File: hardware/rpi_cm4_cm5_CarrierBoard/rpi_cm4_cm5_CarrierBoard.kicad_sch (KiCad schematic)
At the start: 14 parts, among them J21 61300311121, J22 61300311121, U37 SN74LVC1G14DBVR

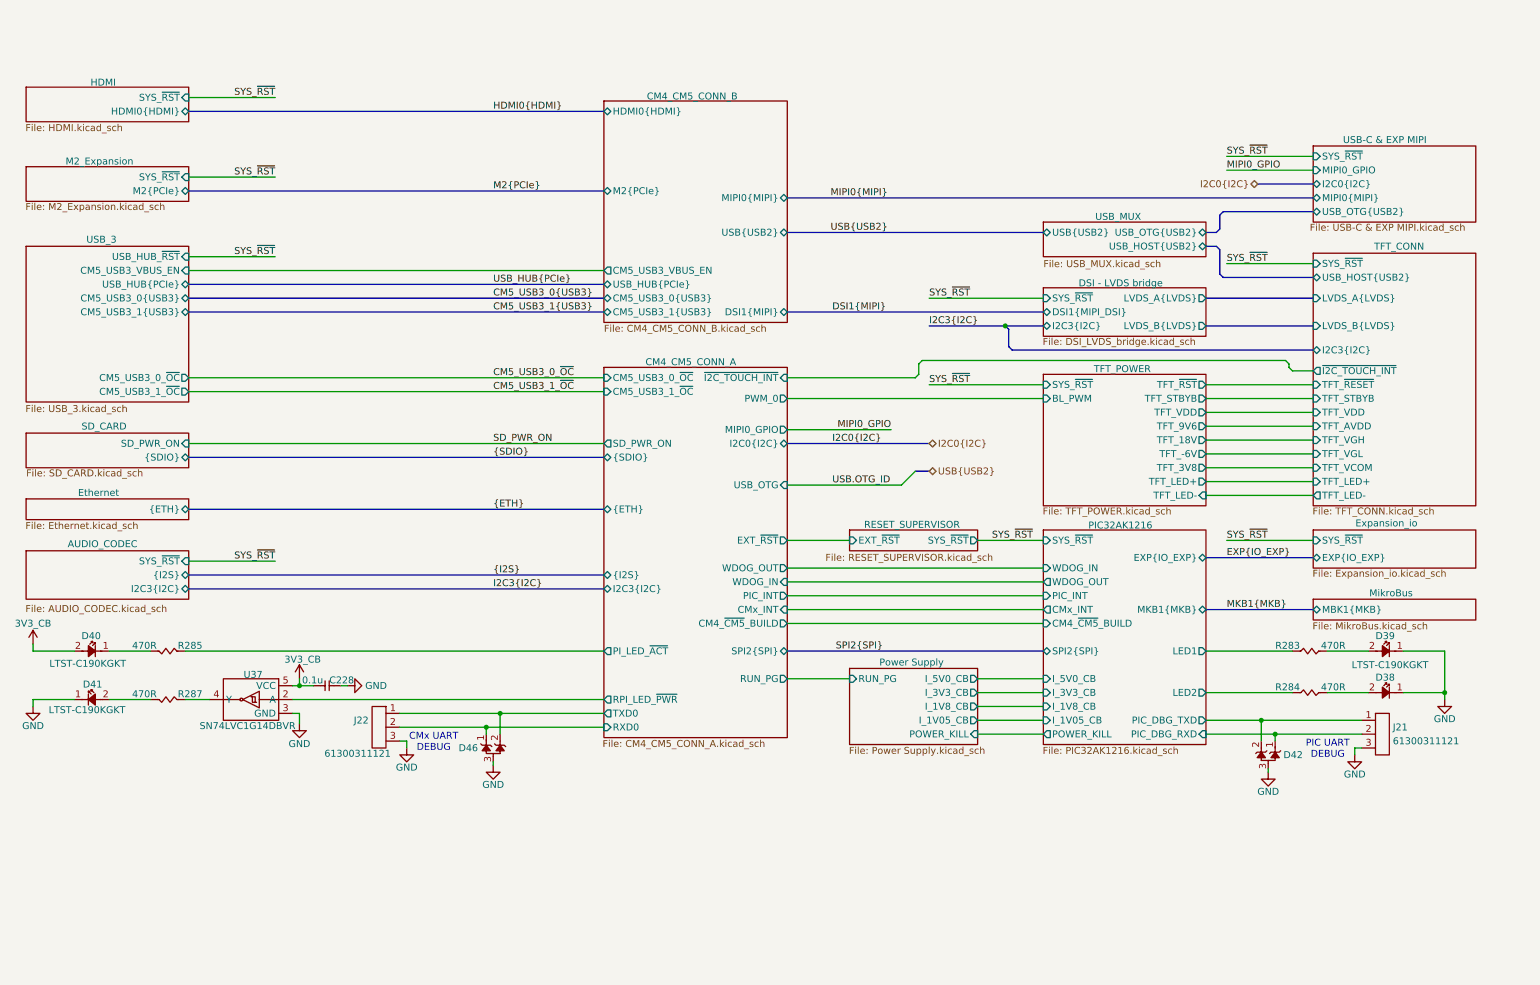
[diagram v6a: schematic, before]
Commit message: Added power input protection & filter Added dedicated QWIIC connector on RPI CMx I2C6 bus Adjusted power table and PinMux Updated schematics accordingly
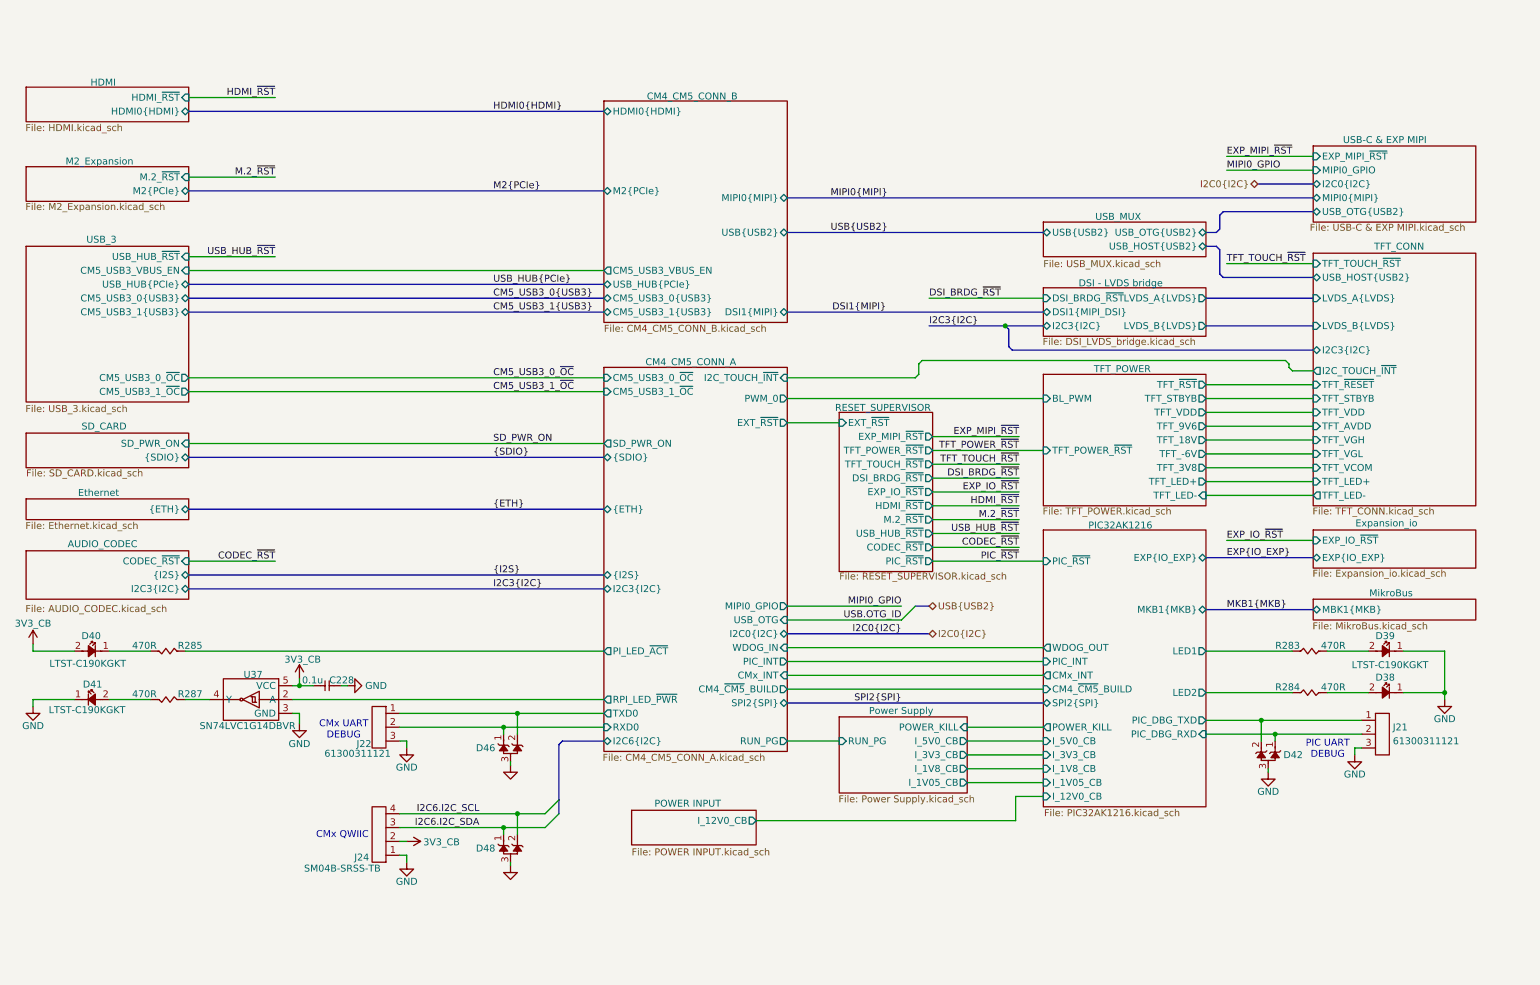
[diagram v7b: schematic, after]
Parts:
- added D48: D1213A-02SOL-7, footprint:SOT-23-3, symbol KicadCompDb:ESD Diodes/ESD_DIODE_00002
- added J24: SM04B-SRSS-TB, footprint:SM04B-SRSS-TB, symbol KicadCompDb:Connector/ONN_00023
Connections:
- net 3V3_CB: now also J24.2
- net GND: now also D48.3 (GND), J24.1
- new net I2C6.I2C_SCL: D48.2 (A), J24.4
- new net I2C6.I2C_SDA: D48.1, J24.3
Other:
- added sheet POWER INPUT (POWER INPUT.kicad_sch)
- sheet AUDIO_CODEC ports: added CODEC_~{RST}; removed SYS_~{RST}
- sheet CM4_CM5_CONN_A ports: added I2C6{I2C}, I2C_TOUCH_~{INT}; removed WDOG_OUT, ~{I2C_TOUCH_INT}
- sheet DSI - LVDS bridge ports: added DSI_BRDG_~{RST}; removed SYS_~{RST}
- sheet Expansion_io ports: added EXP_IO_~{RST}; removed SYS_~{RST}
- sheet HDMI ports: added HDMI_~{RST}; removed SYS_~{RST}
- sheet M2_Expansion ports: added M.2_~{RST}; removed SYS_~{RST}
- sheet PIC32AK1216 ports: added I_12V0_CB, PIC_~{RST}; removed SYS_~{RST}, WDOG_IN
- sheet RESET_SUPERVISOR ports: added CODEC_~{RST}, DSI_BRDG_~{RST}, EXP_IO_~{RST}, EXP_MIPI_~{RST}, HDMI_~{RST}, M.2_~{RST}, PIC_~{RST}, TFT_POWER_~{RST}, TFT_TOUCH_~{RST}, USB_HUB_~{RST}; removed SYS_~{RST}
- sheet TFT_CONN ports: added I2C_TOUCH_~{INT}, TFT_TOUCH_~{RST}; removed SYS_~{RST}, ~{I2C_TOUCH_INT}
- sheet TFT_POWER ports: added TFT_POWER_~{RST}; removed SYS_~{RST}
- sheet USB-C & EXP MIPI ports: added EXP_MIPI_~{RST}; removed SYS_~{RST}
- note added: "CMx QWIIC"
- moved on the sheet: D46

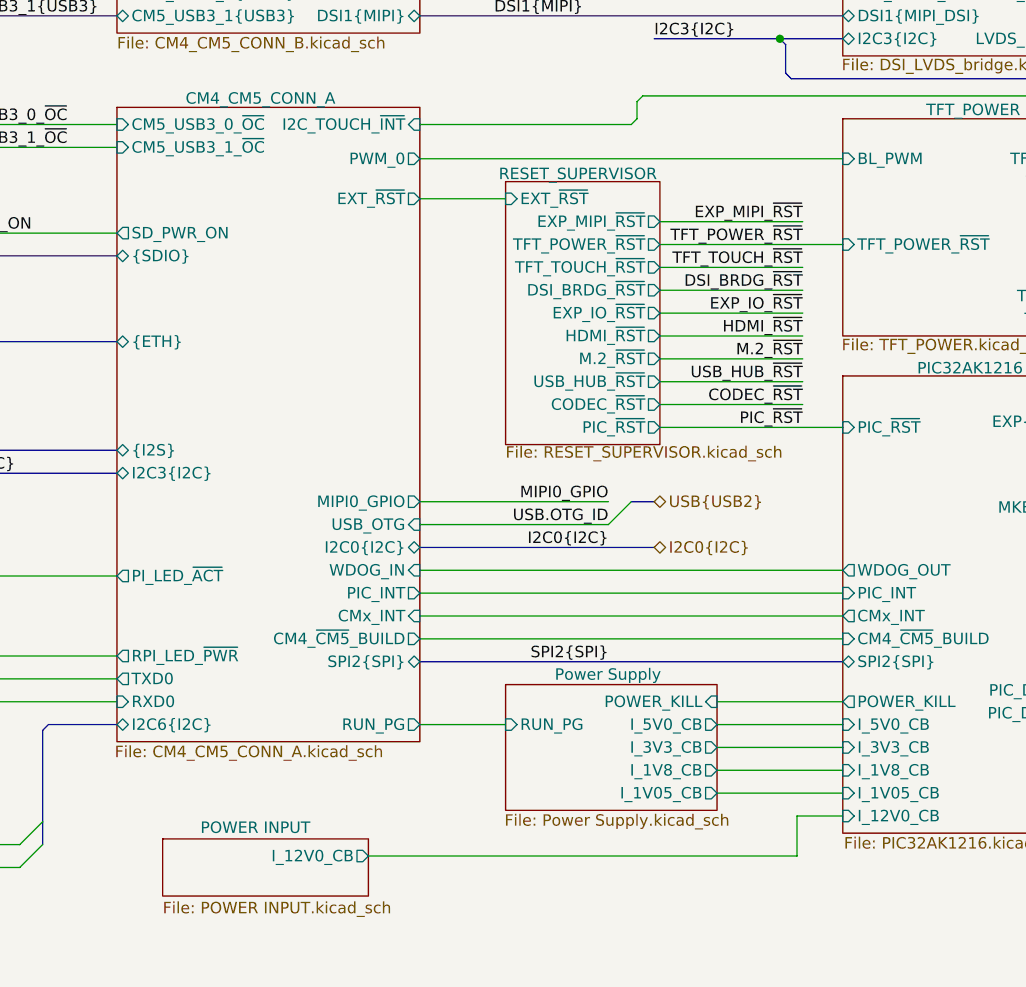
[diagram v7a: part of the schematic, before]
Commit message: Review watchdog timer circuit to prevent race condition during shutdown
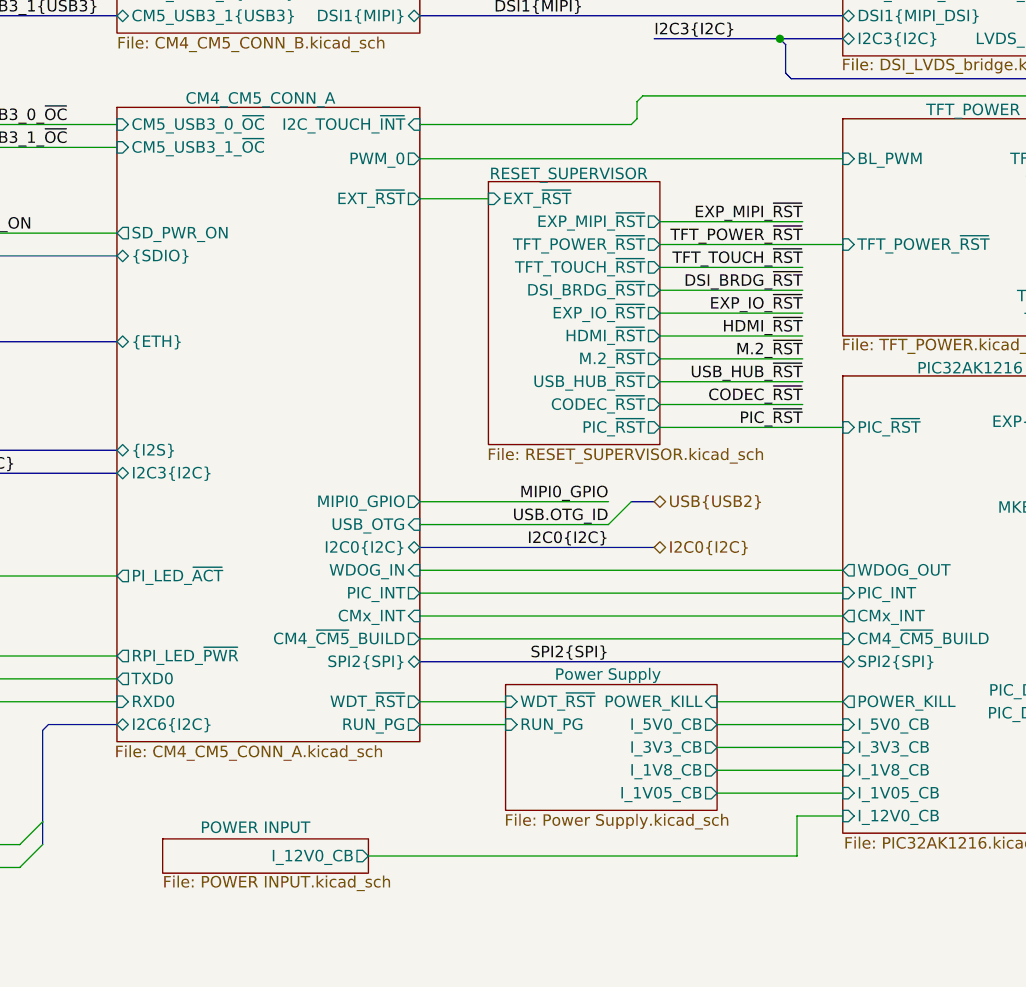
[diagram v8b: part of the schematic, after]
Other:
- sheet CM4_CM5_CONN_A ports: added WDT_~{RST}; removed none
- sheet Power Supply ports: added WDT_~{RST}; removed none
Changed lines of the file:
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@@
 	(wire
 		(pts
-			(xy 155.575 87.63) (xy 165.1 87.63)
-		)
-		(stroke
-			(width 0)
-			(type default)
-		)
-	)
-	(wire
-		(pts
 			(xy 236.22 38.735) (xy 252.095 38.735)
 		)
@@
 	(wire
 		(pts
+			(xy 155.575 143.51) (xy 165.1 143.51)
+		)
+		(stroke
+			(width 0)
+			(type default)
+		)
+	)
+	(wire
+		(pts
 			(xy 45.72 91.44) (xy 121.92 91.44)
 		)
@@
 		)
 	)
+	(wire
+		(pts
+			(xy 155.575 87.63) (xy 163.195 87.63)
+		)
+		(stroke
+			(width 0)
+			(type default)
+		)
+	)
 	(bus
 		(pts
@@
 	(sheet
 		(at 127 158.75)
-		(size 22.86 6.35)
+		(size 22.86 3.81)
 		(exclude_from_sim no)
 		(in_bom yes)
@@
 		)
 		(property "Sheetfile" "POWER INPUT.kicad_sch"
-			(at 127 165.6846 0)
+			(at 127 162.814 0)
 			(effects
 				(font
@@
 			)
 		)
+		(pin "WDT_~{RST}" input
+			(at 165.1 143.51 180)
+			(effects
+				(font
+					(size 1.27 1.27)
+				)
+				(justify left)
+			)
+		)
 		(instances
 			(project "rpi_cm4_cm5_CarrierBoard"
@@
 			)
 		)
+		(pin "WDT_~{RST}" output
+			(at 155.575 143.51 0)
+			(effects
+				(font
+					(size 1.27 1.27)
+				)
+				(justify right)
+			)
+		)
 		(instances
 			(project "rpi_cm4_cm5_CarrierBoard"
@@
 	)
 	(sheet
-		(at 165.1 85.725)
-		(size 17.145 29.21)
+		(at 163.195 85.725)
+		(size 19.05 29.21)
 		(exclude_from_sim no)
 		(in_bom yes)
@@
 		)
 		(property "Sheetname" "RESET_SUPERVISOR"
-			(at 164.338 85.598 0)
+			(at 163.322 85.598 0)
 			(effects
 				(font
@@
 		)
 		(property "Sheetfile" "RESET_SUPERVISOR.kicad_sch"
-			(at 165.1 115.062 0)
+			(at 163.068 115.316 0)
 			(effects
 				(font
@@
 		)
 		(pin "EXT_~{RST}" input
-			(at 165.1 87.63 180)
+			(at 163.195 87.63 180)
 			(effects
 				(font
